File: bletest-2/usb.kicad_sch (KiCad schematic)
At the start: 8 parts, among them J7 USB_C_Receptacle_USB2.0_16P

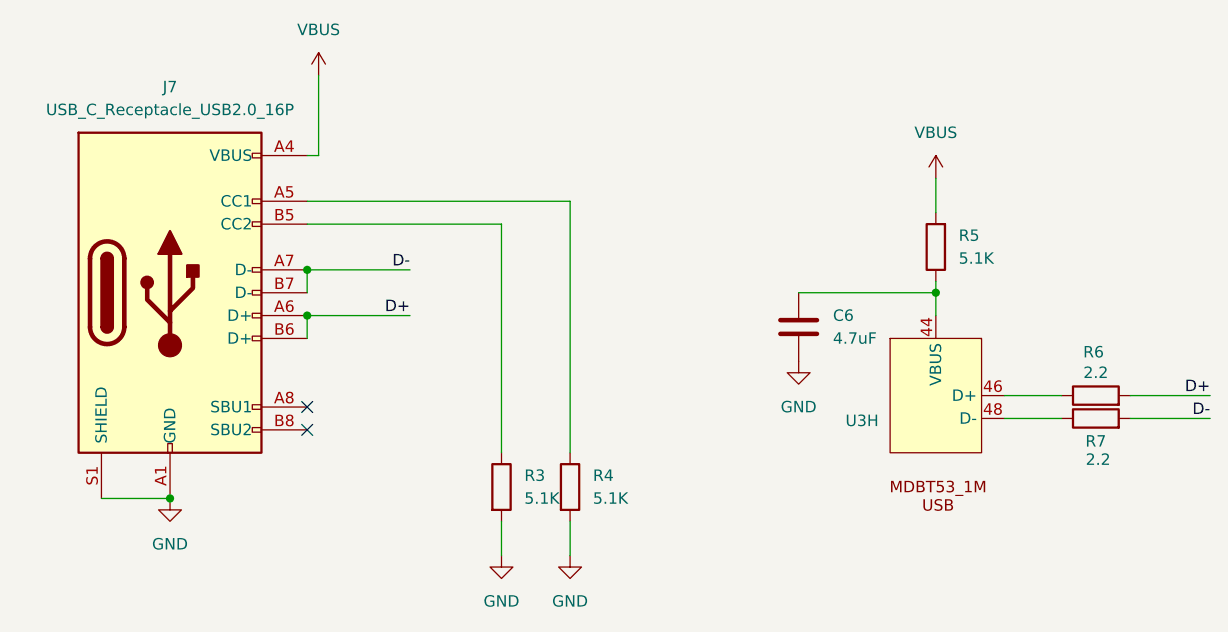
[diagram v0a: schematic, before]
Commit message: Full routing done
There are still a bunch of ERC violations.
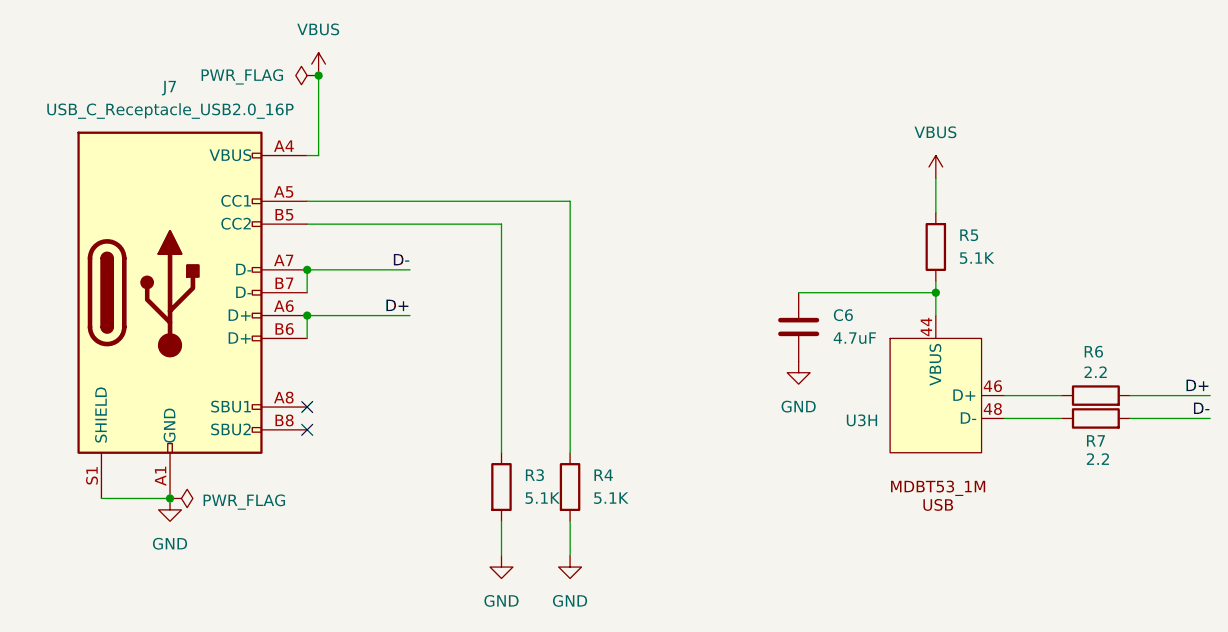
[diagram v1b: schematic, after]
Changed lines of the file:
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@@
+	)
+	(junction
+		(at 78.74 40.64)
+		(diameter 0)
+		(color 0 0 0 0)
 	)
 	(junction
@@
 		(pin "16"
 		)
-		(pin "21"
-		)
-		(pin "23"
-		)
-		(pin "26"
-		)
 		(pin "27"
 		)
@@
 		(pin "13"
 		)
+		(pin "15"
+		)
+		(pin "18"
+		)
+		(pin "29"
+		)
+		(pin "30"
+		)
+		(pin "32"
+		)
+		(pin "44"
+		)
+		(pin "46"
+		)
+		(pin "48"
+		)
+		(pin "55"
+		)
+		(pin "59"
+		)
+		(pin "63"
+		)
+		(pin "64"
+		)
+		(pin "24"
+		)
+		(pin "54"
+		)
+		(pin "61"
+		)
+		(pin "41"
+		)
+		(pin "58"
+		)
+		(pin "50"
+		)
+		(pin "40"
+		)
+		(pin "42"
+		)
+		(pin "52"
+		)
+		(pin "38"
+		)
 		(pin "14"
-		)
-		(pin "15"
-		)
-		(pin "16"
-		)
-		(pin "17"
-		)
-		(pin "18"
-		)
-		(pin "27"
-		)
-		(pin "28"
-		)
-		(pin "29"
-		)
-		(pin "30"
-		)
-		(pin "32"
-		)
-		(pin "39"
-		)
-		(pin "5"
-		)
-		(pin "60"
-		)
-		(pin "7"
-		)
-		(pin "9"
-		)
-		(pin "44"
-		)
-		(pin "46"
-		)
-		(pin "48"
-		)
-		(pin "55"
-		)
-		(pin "59"
-		)
-		(pin "63"
-		)
-		(pin "64"
-		)
-		(pin "20"
-		)
-		(pin "35"
-		)
-		(pin "37"
-		)
-		(pin "24"
-		)
-		(pin "54"
-		)
-		(pin "61"
-		)
-		(pin "41"
-		)
-		(pin "58"
-		)
-		(pin "50"
-		)
-		(pin "40"
-		)
-		(pin "42"
-		)
-		(pin "52"
-		)
-		(pin "38"
 		)
 		(instances
@@
 					(reference "U3")
 					(unit 8)
+				)
+			)
+		)
+	)
+	(symbol
+		(lib_id "power:PWR_FLAG")
+		(at 78.74 40.64 90)
+		(unit 1)
+		(exclude_from_sim no)
+		(in_bom yes)
+		(on_board yes)
+		(dnp no)
+		(fields_autoplaced yes)
+		(property "Reference" "#FLG06"
+			(at 76.835 40.64 0)
+			(effects
+				(font
+					(size 1.27 1.27)
+				)
+				(hide yes)
+			)
+		)
+		(property "Value" "PWR_FLAG"
+			(at 74.93 40.6399 90)
+			(effects
+				(font
+					(size 1.27 1.27)
+				)
+				(justify left)
+			)
+		)
+		(property "Footprint" ""
+			(at 78.74 40.64 0)
+			(effects
+				(font
+					(size 1.27 1.27)
+				)
+				(hide yes)
+			)
+		)
+		(property "Datasheet" "~"
+			(at 78.74 40.64 0)
+			(effects
+				(font
+					(size 1.27 1.27)
+				)
+				(hide yes)
+			)
+		)
+		(property "Description" "Special symbol for telling ERC where power comes from"
+			(at 78.74 40.64 0)
+			(effects
+				(font
+					(size 1.27 1.27)
+				)
+				(hide yes)
+			)
+		)
+		(pin "1"
+		)
+		(instances
+			(project "bletest-2"
+				(path "/8765e634-cc5d-4e93-a9fe-a7a0a02791b6/d969b4c7-11b2-4515-8bee-84969bda5dbe"
+					(reference "#FLG06")
+					(unit 1)
 				)
 			)
@@
 					(unit 1)
 				)
+			)
+		)
+	)
+	(symbol
+		(lib_id "power:PWR_FLAG")
+		(at 62.23 87.63 270)
+		(unit 1)
+		(exclude_from_sim no)
+		(in_bom yes)
+		(on_board yes)
+		(dnp no)
+		(property "Reference" "#FLG07"
+			(at 64.135 87.63 0)
+			(effects
+				(font
+					(size 1.27 1.27)
+				)
+				(hide yes)
+			)
+		)
+		(property "Value" "PWR_FLAG"
+			(at 65.786 87.884 90)
+			(effects
+				(font
+					(size 1.27 1.27)
+				)
+				(justify left)
+			)
+		)
+		(property "Footprint" ""
+			(at 62.23 87.63 0)
+			(effects
+				(font
+					(size 1.27 1.27)
+				)
+				(hide yes)
+			)
+		)
+		(property "Datasheet" "~"
+			(at 62.23 87.63 0)
+			(effects
+				(font
+					(size 1.27 1.27)
+				)
+				(hide yes)
+			)
+		)
+		(property "Description" "Special symbol for telling ERC where power comes from"
+			(at 62.23 87.63 0)
+			(effects
+				(font
+					(size 1.27 1.27)
+				)
+				(hide yes)
+			)
+		)
+		(pin "1"
+		)
+		(instances
+			(project "bletest-2"
+				(path "/8765e634-cc5d-4e93-a9fe-a7a0a02791b6/d969b4c7-11b2-4515-8bee-84969bda5dbe"
+					(reference "#FLG07")
+					(unit 1)
+				)

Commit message: Rev A of bletest
Finish cleanup, and remove last remaining violations.

There are a handful of silkscreen overlaps with explicit exclusions.
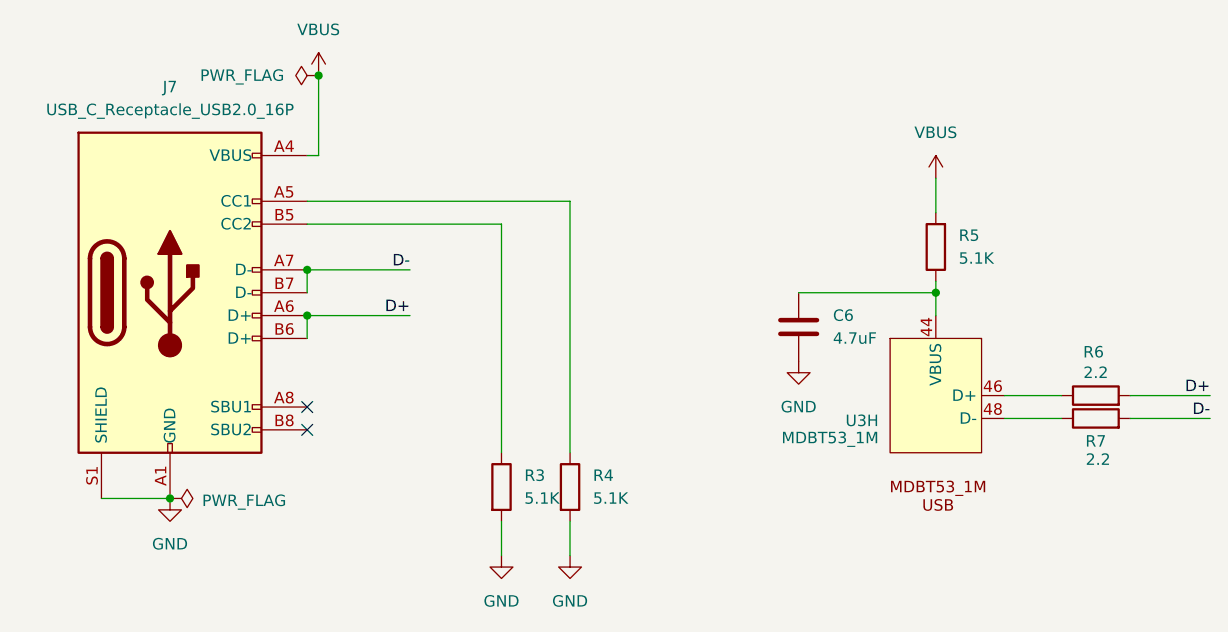
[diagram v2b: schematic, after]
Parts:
- U3: value ~ -> MDBT53_1M
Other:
- company: (none) -> David Brown
- title: (none) -> BLETEXT-2
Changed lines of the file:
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@@
 	(generator "eeschema")
 	(generator_version "8.0")
-	(paper "A4")
+	(paper "A")
+	(title_block
+		(title "BLETEXT-2")
+		(date "2024-12-07")
+		(rev "REVA")
+		(company "David Brown")
+	)
 	(junction
 		(at 77.47 67.31)
@@
 			)
 		)
-		(property "Datasheet" "~"
+		(property "Datasheet" "https://www.digikey.com/en/products/detail/panasonic-electronic-components/ERJ-3GEYJ2R2V/282119"
 			(at 165.1 76.2 0)
 			(effects
@@
 			)
 		)
-		(property "Datasheet" "~"
+		(property "Datasheet" "https://www.digikey.com/en/products/detail/yageo/RC0603JR-075K1L/726796"
 			(at 106.68 86.36 0)
 			(effects
@@
 			)
 		)
-		(property "Datasheet" "~"
+		(property "Datasheet" "https://www.digikey.com/en/products/detail/yageo/RC0603JR-075K1L/726796"
 			(at 147.32 59.69 0)
 			(effects
@@
 			)
 		)
-		(property "Datasheet" "https://www.usb.org/sites/default/files/documents/usb_type-c.zip"
+		(property "Datasheet" "https://www.digikey.com/en/products/detail/gct/USB4085-GF-A/9859662"
 			(at 66.04 64.77 0)
 			(effects
@@
 			)
 		)
-		(property "Value" "~"
+		(property "Value" "MDBT53_1M"
 			(at 140.97 80.905 0)
 			(effects
@@
 			)
 		)
-		(property "Datasheet" ""
+		(property "Datasheet" "https://www.amazon.com/dp/B0B4BC8Z1V"
 			(at 147.32 78.74 0)
 			(effects
@@
 			)
 		)
-		(property "Datasheet" "~"
+		(property "Datasheet" "https://www.digikey.com/en/products/detail/yageo/RC0603JR-075K1L/726796"
 			(at 99.06 86.36 0)
 			(effects
@@
 			)
 		)
-		(property "Datasheet" "~"
+		(property "Datasheet" "https://www.digikey.com/en/products/detail/panasonic-electronic-components/ERJ-3GEYJ2R2V/282119"
 			(at 165.1 78.74 0)
 			(effects
@@
 			)
 		)
-		(property "Datasheet" "~"
+		(property "Datasheet" "https://www.digikey.com/en/products/detail/samsung-electro-mechanics/CL10A475KP8NNNC/3886702"
 			(at 132.08 68.58 0)
 			(effects
